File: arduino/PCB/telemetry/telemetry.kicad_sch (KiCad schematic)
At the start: 3 parts, among them U1 MEGA_PRO_EMBED_CH340G_{slash}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, U2 NEO-M8N

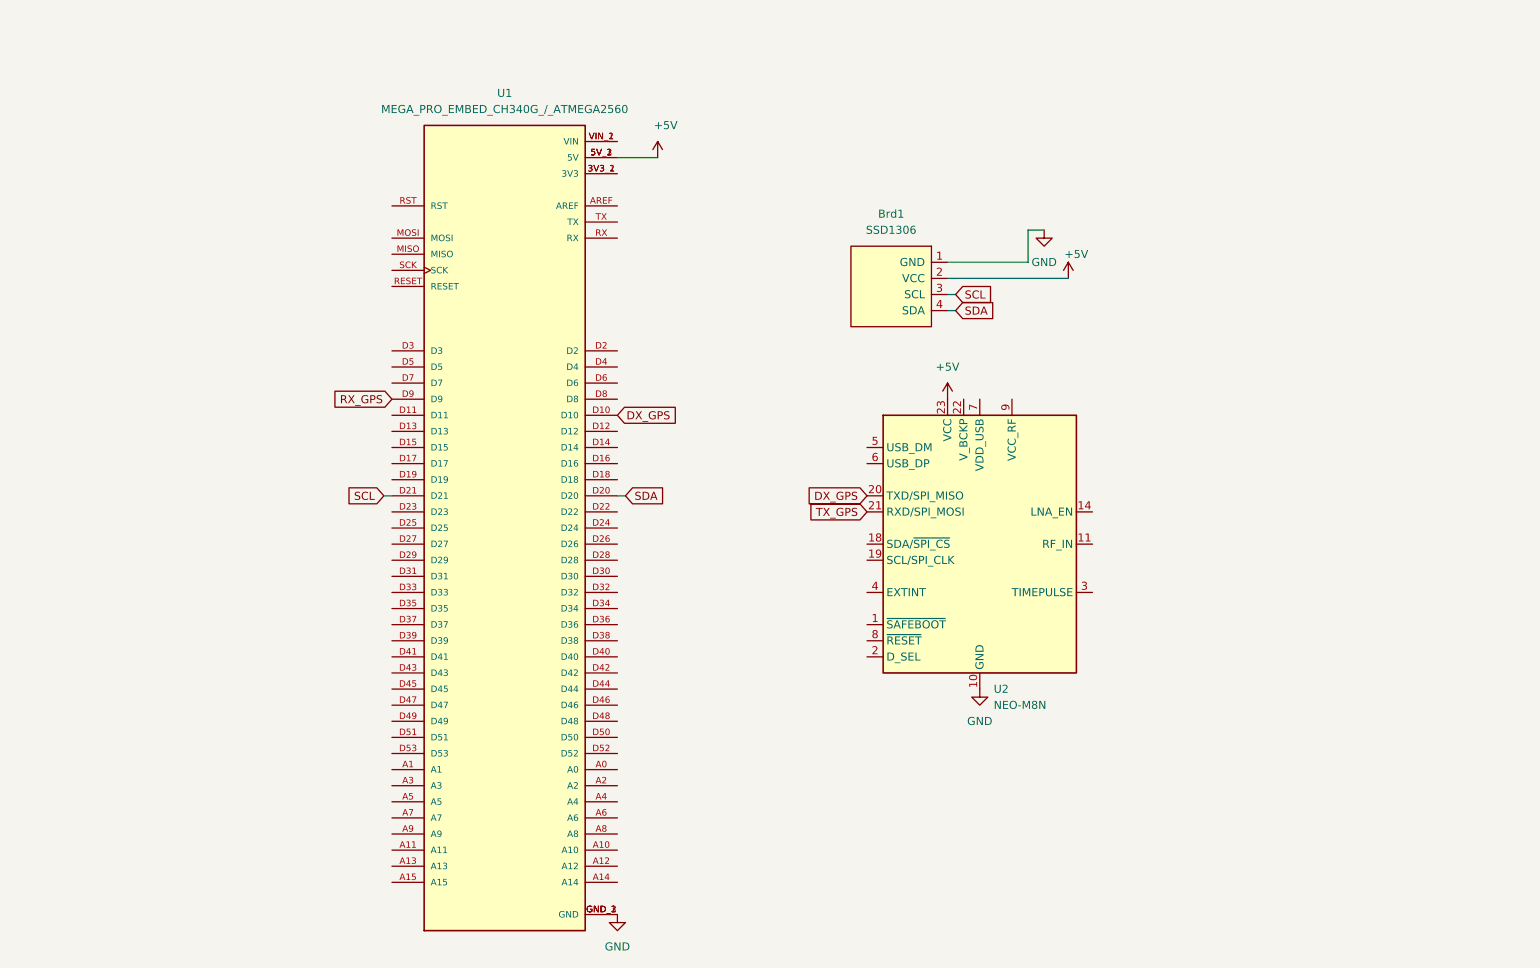
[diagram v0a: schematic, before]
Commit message: Add Feature of Revolutions
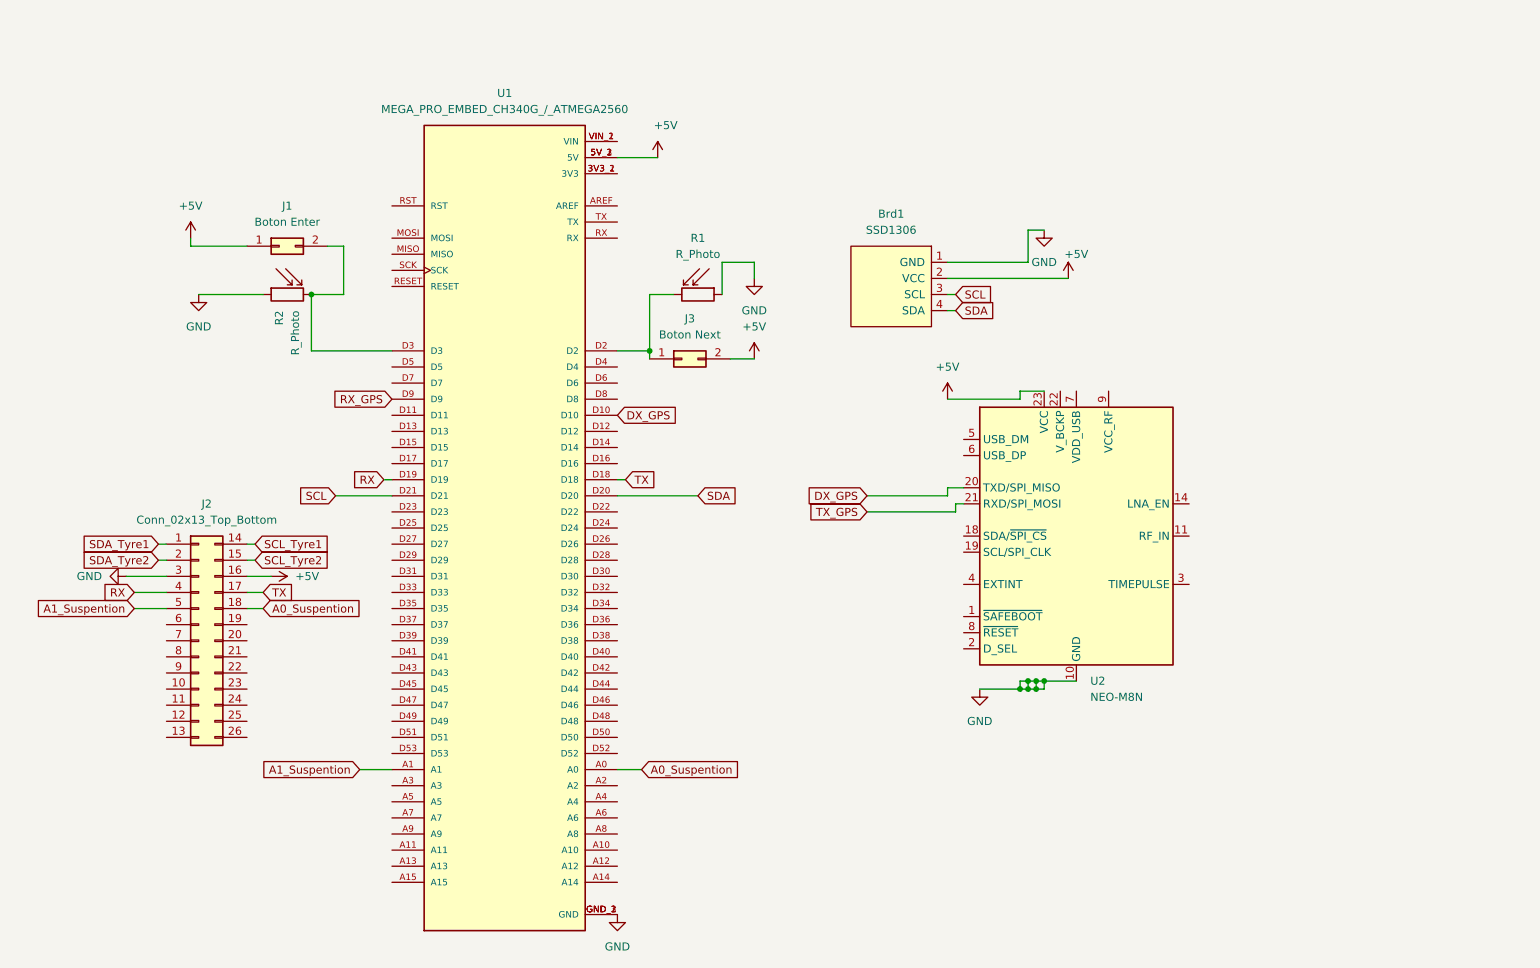
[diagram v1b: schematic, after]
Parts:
- added J1: Boton Enter, Button_Switch_SMD:SW_SPST_EVPBF, symbol Connector_Generic:Conn_02x01
- added J2: Conn_02x13_Top_Bottom, symbol Connector_Generic:Conn_02x13_Top_Bottom
- added J3: Boton Next, Button_Switch_SMD:SW_SPST_EVPBF, symbol Connector_Generic:Conn_02x01
- added R1, R2: R_Photo, Resistor_THT:R_Axial_DIN0204_L3.6mm_D1.6mm_P7.62mm_Horizontal, symbol Device:R_Photo
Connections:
- net +5V: now also J1.1 (Pin_1), J2.16 (Pin_16), J3.2 (Pin_2)
- net GND: now also J2.3 (Pin_3), R1.1, R2.1
- net A0_Suspention: now reaches U1.A0
- net A0_Suspention: now also J2.18 (Pin_18)
- net A1_Suspention: now reaches U1.A1
- net A1_Suspention: now also J2.5 (Pin_5)
- net TX: now reaches U1.D18
- net TX: now also J2.17 (Pin_17)
- net RX: now reaches U1.D19
- net RX: now also J2.4 (Pin_4)
- net at U1.D2: now also J3.1 (Pin_1), R1.2
- net at U1.D3: now also J1.2 (Pin_2), R2.2
- new net SCL_Tyre1: J2.14 (Pin_14)
- new net SCL_Tyre2: J2.15 (Pin_15)
- new net SDA_Tyre1: J2.1 (Pin_1)
- new net SDA_Tyre2: J2.2 (Pin_2)
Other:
- moved on the sheet: U2

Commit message: Linear Sensor
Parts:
- removed J2: Conn_02x13_Top_Bottom, symbol Connector_Generic:Conn_02x13_Top_Bottom
- added J4: DE9_Plug, Connector_JST:JST_EH_S9B-EH_1x09_P2.50mm_Horizontal, symbol Connector:DE9_Plug
- added U3: CR2013-MI2120, Display:CR2013-MI2120, symbol Driver_Display:CR2013-MI2120
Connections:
- net DX_GPS is gone; now on net TX_GPS: U1.D10, U2.20 (TXD/SPI_MISO)
- net +5V: now also J4.9, U3.1 (VCC)
- net A0_Suspention: now also J4.6
- net A1_Suspention: now also J4.7
- net GND: now also J4.5, U3.2 (GND)
- net RX_GPS: now also U2.21 (RXD/SPI_MOSI)
- net SCL: now also J4.1
- net SDA: now also J4.2
- net TX_GPS: no longer U2.21 (RXD/SPI_MOSI)
- net DC: now reaches U1.D29
- net DC: now also U3.5 (D/~{C}), U3.9 (MISO)
- net CS: now reaches U1.D30
- net CS: now also U3.3 (~{CS})
- net RST: now reaches U1.D31
- net RST: now also U3.4 (RESET)
- net at U1.MOSI: now also U3.6 (MOSI)
- net at U1.SCK: now also U3.7 (SCK)
- net VIN_2: now reaches U1.VIN_1 (VIN), U1.VIN_2 (VIN)
- net VIN_2: now also J4.8
- net RX renamed RPM
- net RPM: now also J4.3
- net TX: no longer names the net of U1.D18
- new net +3.3V: U3.8 (LED)
- new net +8V: J4.4
